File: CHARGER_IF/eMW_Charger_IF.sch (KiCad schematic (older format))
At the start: 9 parts

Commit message: Charger IF WIP
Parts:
- removed U?: SN74ACT08N, symbol SN74LS08N
- added C?: 10 uF / 25V / TH, symbol C
- added C?: 22 uF / 16V / TH, symbol C
- added J?: Booster_J1_J3, symbol Booster_J1_J3
- added J?: Booster_J4_J2, symbol Booster_J4_J2
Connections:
- net +5V: now also U?.12 (4A), U?.9 (3A), C?.1, J?.21 (P21)
- net 12V: now also C?.1
- net GND: now also U?.7 (GND), C?.2, C?.2, J?.22 (P22)
- net at U?.23 (RXI): now also J?.3 (P3)
- net at U?.24 (TXO): now also J?.4 (P4)
- net at U?.31 (A4-T2): now also J?.25 (P25)
- net at U?.32 (A5-MainsV): now also J?.26 (P26)
- net at U?.33 (A6-Analog-Spare-1): now also J?.27 (P27)
- net at U?.34 (A7-Analog-Spare-2): now also J?.28 (P28)
- net at U?.5 (A3-Uvio): now also J?.24 (P24)
- net at U?.7 (A1-V-Sense): now also J?.2 (P2)
- net at U?.8 (A0-C-Sense): now also J?.6 (P6)
- net at U?.~ (A2-Heat-Sink-Temp): now also J?.23 (P23)
- net at U?.12 (4A): now also J?.36 (P36)
- net at U?.2 (1B): now also J?.38 (P38)
- net at U?.5 (2B): now also J?.37 (P37)
- net at U?.9 (3A): now also J?.35 (P35)
- net at U?.2 (1B): now also J?.34 (P34)
- net at U?.5 (2B): now also J?.33 (P33)
- net at R?.1, R?.2: now also J?.39 (P39)
- net at R?.1, R?.2: now also J?.40 (P40)
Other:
- moved on the sheet: R?, U?

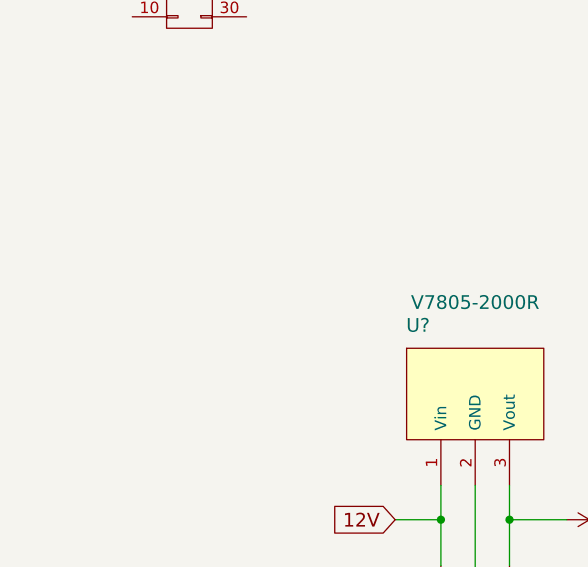
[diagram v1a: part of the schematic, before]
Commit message: Added URLS WIP
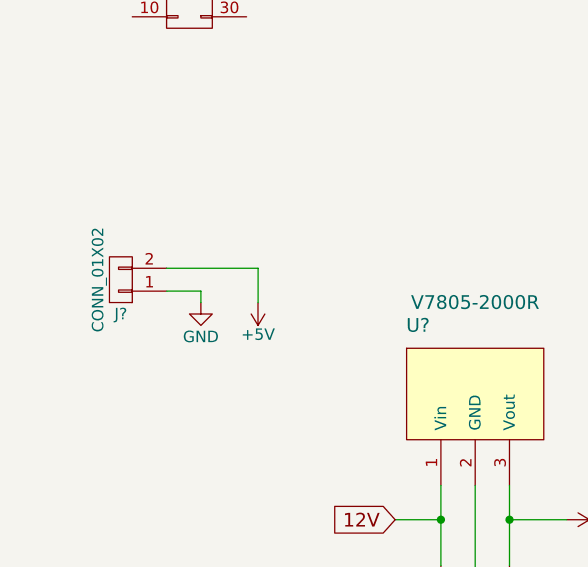
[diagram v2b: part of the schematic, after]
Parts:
- added J?: CONN_01X02, symbol CONN_01X02
- C?: Mouser PN (none) -> 810-FG26X7R1E106KRT6; Mouser URL (none) -> http://www.mouser.com/search/ProductDetail.aspx?R=0virtualk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
- C?: Mouser PN (none) -> 810-FG22X7R1E226MRT6; Mouser URL (none) -> http://www.mouser.com/search/ProductDetail.aspx?R=0virtualk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
- U? (x2): Mouser PN (none) -> 595-SN74ACT08N; Mouser URL (none) -> http://www.mouser.com/search/ProductDetail.aspx?R=0virtualk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
- U?: Mouser PN (none) -> 490-V7805-2000R; Mouser URL (none) -> http://www.mouser.com/search/ProductDetail.aspx?R=0virtualk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
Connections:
- net +5V: now also J?.2 (P2)
- net GND: now also J?.1 (P1)
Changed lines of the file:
@@
 F 2 "" H 7000 2700 60  0000 C CNN
 F 3 "" H 7000 2700 60  0000 C CNN
+F 4 "595-SN74ACT08N" H 7000 2700 60  0001 C CNN "Mouser PN"
+F 5 "http://www.mouser.com/search/ProductDetail.aspx?R=0virtualkey0virtualkeySN74ACT08N" H 7000 2700 60  0001 C CNN "Mouser URL"
 	1    7000 2700
 	-1   0    0    -1
@@
 F 2 "" H 7000 4850 60  0000 C CNN
 F 3 "" H 7000 4850 60  0000 C CNN
+F 4 "595-SN74ACT08N" H 7000 4850 60  0001 C CNN "Mouser PN"
+F 5 "http://www.mouser.com/search/ProductDetail.aspx?R=0virtualkey0virtualkeySN74ACT08N" H 7000 4850 60  0001 C CNN "Mouser URL"
 	1    7000 4850
 	-1   0    0    -1
@@
 F 2 "" H 2950 4450 60  0000 C CNN
 F 3 "" H 2950 4450 60  0000 C CNN
+F 4 "490-V7805-2000R" H 2950 4450 60  0001 C CNN "Mouser PN"
+F 5 "http://www.mouser.com/search/ProductDetail.aspx?R=0virtualkey0virtualkeyV7805-2000R" H 2950 4450 60  0001 C CNN "Mouser URL"
 	1    2950 4450
 	1    0    0    -1
@@
 F 2 "" H 2838 5200 50  0000 C CNN
 F 3 "" H 2800 5350 50  0000 C CNN
+F 4 "810-FG26X7R1E106KRT6" H 2800 5350 60  0001 C CNN "Mouser PN"
+F 5 "http://www.mouser.com/search/ProductDetail.aspx?R=0virtualkey0virtualkeyFG26X7R1E106KRT06" H 2800 5350 60  0001 C CNN "Mouser URL"
 	1    2800 5350
 	1    0    0    -1
@@
 F 2 "" H 3138 5200 50  0000 C CNN
 F 3 "" H 3100 5350 50  0000 C CNN
+F 4 "810-FG22X7R1E226MRT6" H 3100 5350 60  0001 C CNN "Mouser PN"
+F 5 "http://www.mouser.com/search/ProductDetail.aspx?R=0virtualkey0virtualkeyFG22X7R1E226MRT06" H 3100 5350 60  0001 C CNN "Mouser URL"
 	1    3100 5350
 	1    0    0    -1
@@
 	7600 5050 7950 5050
 Connection ~ 7950 5050
+$Comp
+L CONN_01X02 J?
+U 1 1 59765191
+P 1400 3950
+F 0 "J?" H 1400 4100 50  0000 C CNN
+F 1 "CONN_01X02" V 1500 3950 50  0000 C CNN
+F 2 "" H 1400 3950 50  0001 C CNN
+F 3 "" H 1400 3950 50  0001 C CNN
+	1    1400 3950
+	-1   0    0    1
+$EndComp
+$Comp
+L GND #PWR?
+U 1 1 597651CE
+P 1750 4050
+F 0 "#PWR?" H 1750 3800 50  0001 C CNN
+F 1 "GND" H 1750 3900 50  0000 C CNN
+F 2 "" H 1750 4050 50  0001 C CNN
+F 3 "" H 1750 4050 50  0001 C CNN
+	1    1750 4050
+	1    0    0    -1
+$EndComp
+$Comp
+L +5V #PWR?
+U 1 1 597651FC
+P 2000 4050
+F 0 "#PWR?" H 2000 3900 50  0001 C CNN
+F 1 "+5V" H 2000 4190 50  0000 C CNN
+F 2 "" H 2000 4050 50  0001 C CNN
+F 3 "" H 2000 4050 50  0001 C CNN
+	1    2000 4050
+	-1   0    0    1
+$EndComp
+Wire Wire Line
+	1750 4050 1750 4000
+Wire Wire Line
+	1750 4000 1600 4000
+Wire Wire Line
+	1600 3900 2000 3900
+Wire Wire Line
+	2000 3900 2000 4050
 $EndSCHEMATC

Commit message: Rough start on charger IF PCB
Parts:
- C1, C2: renamed from C?; footprint (none) -> Capacitors_THT:CP_Radial_D6.3mm_P2.50mm
- J1: renamed from J?; footprint (none) -> Pin_Headers:Pin_Header_Straight_1x02_Pitch2.54mm
- J2: renamed from J?; footprint (none) -> eMW_Charger:6-146256-0
- J3: renamed from J?; footprint (none) -> eMW_Charger:6-146256-0_40-31_20_11
- R1, R2, R3, R4: renamed from R?; footprint (none) -> Resistors_THT:R_Axial_DIN0204_L3.6mm_D1.6mm_P5.08mm_Horizontal
- U1: renamed from U?; footprint (none) -> eMW_Charger:V7805-2000R
- U2: renamed from U?; footprint (none) -> Pin_Headers:Pin_Header_Straight_2x10_Pitch2.54mm
- U3, U4: renamed from U?; footprint (none) -> Housings_DIP:DIP-14_W7.62mm
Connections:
- net +5V: no longer J1.2 (P2)
- net 12V renamed +12V
- net +12V: now also J1.2 (P2)
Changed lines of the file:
@@
 $EndDescr
 $Comp
-L ArduinoSocket U?
+L ArduinoSocket U2
 U 1 1 59742778
 P 4500 1850
-F 0 "U?" H 5250 2800 60  0000 C CNN
+F 0 "U2" H 5250 2800 60  0000 C CNN
 F 1 "ArduinoSocket" H 3900 2800 60  0000 C CNN
-F 2 "" H 4500 1500 60  0000 C CNN
+F 2 "Pin_Headers:Pin_Header_Straight_2x10_Pitch2.54mm" H 4500 1500 60  0001 C CNN
 F 3 "" H 4500 1500 60  0000 C CNN
 	1    4500 1850
@@
 $EndComp
 $Comp
-L SN74LS08N U?
+L SN74LS08N U3
 U 1 1 59742C3C
 P 7000 2700
-F 0 "U?" H 7200 3400 60  0000 C CNN
+F 0 "U3" H 7200 3400 60  0000 C CNN
 F 1 "SN74ACT08N" H 6600 3400 60  0000 C CNN
-F 2 "" H 7000 2700 60  0000 C CNN
+F 2 "Housings_DIP:DIP-14_W7.62mm" H 7000 2700 60  0001 C CNN
 F 3 "" H 7000 2700 60  0000 C CNN
 F 4 "595-SN74ACT08N" H 7000 2700 60  0001 C CNN "Mouser PN"
@@
 $EndComp
 $Comp
-L SN74LS08N U?
+L SN74LS08N U4
 U 1 1 59742C8F
 P 7000 4850
-F 0 "U?" H 7200 5550 60  0000 C CNN
+F 0 "U4" H 7200 5550 60  0000 C CNN
 F 1 "SN74ACT08N" H 6600 5550 60  0000 C CNN
-F 2 "" H 7000 4850 60  0000 C CNN
+F 2 "Housings_DIP:DIP-14_W7.62mm" H 7000 4850 60  0001 C CNN
 F 3 "" H 7000 4850 60  0000 C CNN
 F 4 "595-SN74ACT08N" H 7000 4850 60  0001 C CNN "Mouser PN"
@@
 $EndComp
 $Comp
-L R R?
+L R R4
 U 1 1 59742F49
 P 9500 2300
-F 0 "R?" H 9600 2250 50  0000 C CNN
+F 0 "R4" H 9600 2250 50  0000 C CNN
 F 1 "20k / 10% / TH" H 9900 2350 50  0000 C CNN
-F 2 "" V 9430 2300 50  0000 C CNN
+F 2 "Resistors_THT:R_Axial_DIN0204_L3.6mm_D1.6mm_P5.08mm_Horizontal" V 9430 2300 50  0001 C CNN
 F 3 "" H 9500 2300 50  0000 C CNN
 	1    9500 2300
@@
 $EndComp
 $Comp
-L R R?
+L R R3
 U 1 1 59742FA5
 P 9500 1700
-F 0 "R?" H 9600 1650 50  0000 C CNN
+F 0 "R3" H 9600 1650 50  0000 C CNN
 F 1 "10k / 10% / TH" H 9900 1750 50  0000 C CNN
-F 2 "" V 9430 1700 50  0000 C CNN
+F 2 "Resistors_THT:R_Axial_DIN0204_L3.6mm_D1.6mm_P5.08mm_Horizontal" V 9430 1700 50  0001 C CNN
 F 3 "" H 9500 1700 50  0000 C CNN
 	1    9500 1700
@@
 $EndComp
 $Comp
-L R R?
+L R R1
 U 1 1 59743279
 P 8600 1800
-F 0 "R?" H 8700 1750 50  0000 C CNN
+F 0 "R1" H 8700 1750 50  0000 C CNN
 F 1 "10k / 10% / TH" H 9000 1850 50  0000 C CNN
-F 2 "" V 8530 1800 50  0000 C CNN
+F 2 "Resistors_THT:R_Axial_DIN0204_L3.6mm_D1.6mm_P5.08mm_Horizontal" V 8530 1800 50  0001 C CNN
 F 3 "" H 8600 1800 50  0000 C CNN
 	1    8600 1800
@@
 $EndComp
 $Comp
-L R R?
+L R R2
 U 1 1 597432A0
 P 8600 2300
-F 0 "R?" H 8700 2250 50  0000 C CNN
+F 0 "R2" H 8700 2250 50  0000 C CNN
 F 1 "20k / 10% / TH" H 9000 2350 50  0000 C CNN
-F 2 "" V 8530 2300 50  0000 C CNN
+F 2 "Resistors_THT:R_Axial_DIN0204_L3.6mm_D1.6mm_P5.08mm_Horizontal" V 8530 2300 50  0001 C CNN
 F 3 "" H 8600 2300 50  0000 C CNN
 	1    8600 2300
@@
 $EndComp
 $Comp
-L V7805-2000R U?
+L V7805-2000R U1
 U 1 1 5974381A
 P 2950 4450
-F 0 "U?" H 2700 4750 60  0000 C CNN
+F 0 "U1" H 2700 4750 60  0000 C CNN
 F 1 "V7805-2000R" H 2950 4850 60  0000 C CNN
-F 2 "" H 2950 4450 60  0000 C CNN
+F 2 "eMW_Charger:V7805-2000R" H 2950 4450 60  0001 C CNN
 F 3 "" H 2950 4450 60  0000 C CNN
 F 4 "490-V7805-2000R" H 2950 4450 60  0001 C CNN "Mouser PN"
@@
 	1    0    0    -1
 $EndComp
-Text GLabel 2600 5000 0    60   Input ~ 0
-12V
-$Comp
-L GND #PWR?
+$Comp
+L GND #PWR01
 U 1 1 5974397D
 P 2950 5750
-F 0 "#PWR?" H 2950 5500 50  0001 C CNN
+F 0 "#PWR01" H 2950 5500 50  0001 C CNN
 F 1 "GND" H 2950 5600 50  0000 C CNN
 F 2 "" H 2950 5750 50  0000 C CNN
@@
 $EndComp
 $Comp
-L +5V #PWR?
+L +5V #PWR02
 U 1 1 59743A17
 P 3350 5000
-F 0 "#PWR?" H 3350 4850 50  0001 C CNN
+F 0 "#PWR02" H 3350 4850 50  0001 C CNN
 F 1 "+5V" H 3350 5140 50  0000 C CNN
 F 2 "" H 3350 5000 50  0000 C CNN
@@
 $EndComp
 $Comp
-L +5V #PWR?
+L +5V #PWR03
 U 1 1 59743C47
 P 6750 1850
-F 0 "#PWR?" H 6750 1700 50  0001 C CNN
+F 0 "#PWR03" H 6750 1700 50  0001 C CNN
 F 1 "+5V" H 6750 1990 50  0000 C CNN
 F 2 "" H 6750 1850 50  0000 C CNN
@@
 $EndComp
 $Comp
-L +5V #PWR?
+L +5V #PWR04
 U 1 1 59743C6D
 P 6750 4000
-F 0 "#PWR?" H 6750 3850 50  0001 C CNN
+F 0 "#PWR04" H 6750 3850 50  0001 C CNN
 F 1 "+5V" H 6750 4140 50  0000 C CNN
 F 2 "" H 6750 4000 50  0000 C CNN
@@
 $EndComp
 $Comp
-L GND #PWR?
+L GND #PWR05
 U 1 1 59743F57
 P 6750 3600
-F 0 "#PWR?" H 6750 3350 50  0001 C CNN
+F 0 "#PWR05" H 6750 3350 50  0001 C CNN
 F 1 "GND" H 6750 3450 50  0000 C CNN
 F 2 "" H 6750 3600 50  0000 C CNN
@@
 $EndComp
 $Comp
-L +5V #PWR?
+L +5V #PWR06
 U 1 1 597440FC
 P 7950 4350
-F 0 "#PWR?" H 7950 4200 50  0001 C CNN
+F 0 "#PWR06" H 7950 4200 50  0001 C CNN
 F 1 "+5V" H 7950 4490 50  0000 C CNN
 F 2 "" H 7950 4350 50  0000 C CNN
@@
 $EndComp
 $Comp
-L GND #PWR?
+L GND #PWR07
 U 1 1 59744821
 P 9500 2550
-F 0 "#PWR?" H 9500 2300 50  0001 C CNN
+F 0 "#PWR07" H 9500 2300 50  0001 C CNN
 F 1 "GND" H 9500 2400 50  0000 C CNN
 F 2 "" H 9500 2550 50  0000 C CNN
@@
 $EndComp
 $Comp
-L GND #PWR?
+L GND #PWR08
 U 1 1 59744980
 P 3200 2550
-F 0 "#PWR?" H 3200 2300 50  0001 C CNN
+F 0 "#PWR08" H 3200 2300 50  0001 C CNN
 F 1 "GND" H 3200 2400 50  0000 C CNN
 F 2 "" H 3200 2550 50  0000 C CNN
@@
 $EndComp
 $Comp
-L GND #PWR?
+L GND #PWR09
 U 1 1 59744C12
 P 6750 5750
-F 0 "#PWR?" H 6750 5500 50  0001 C CNN
+F 0 "#PWR09" H 6750 5500 50  0001 C CNN
 F 1 "GND" H 6750 5600 50  0000 C CNN
 F 2 "" H 6750 5750 50  0000 C CNN
@@
 $EndComp
 $Comp
-L +5V #PWR?
+L +5V #PWR010
 U 1 1 59744F3B
 P 8000 2100
-F 0 "#PWR?" H 8000 1950 50  0001 C CNN
+F 0 "#PWR010" H 8000 1950 50  0001 C CNN
 F 1 "+5V" H 8000 2240 50  0000 C CNN
 F 2 "" H 8000 2100 50  0000 C CNN
@@
 $EndComp
 $Comp
-L Booster_J1_J3 J?
+L Booster_J1_J3 J2
 U 1 1 59753F21
 P 1700 2350
-F 0 "J?" H 1700 2900 50  0000 C CNN
+F 0 "J2" H 1700 2900 50  0000 C CNN
 F 1 "Booster_J1_J3" V 1700 2350 50  0000 C CNN
-F 2 "" H 1700 1150 50  0001 C CNN
+F 2 "eMW_Charger:6-146256-0" H 1700 1150 50  0001 C CNN
 F 3 "" H 1700 1150 50  0001 C CNN
 	1    1700 2350
@@
 $EndComp
 $Comp
-L Booster_J4_J2 J?
+L Booster_J4_J2 J3
 U 1 1 59753F62
 P 10450 3100
-F 0 "J?" H 10450 3650 50  0000 C CNN
+F 0 "J3" H 10450 3650 50  0000 C CNN
 F 1 "Booster_J4_J2" V 10450 3100 50  0000 C CNN
-F 2 "" H 10450 1900 50  0001 C CNN
+F 2 "eMW_Charger:6-146256-0_40-31_20_11" H 10450 1900 50  0001 C CNN
 F 3 "" H 10450 1900 50  0001 C CNN
 	1    10450 3100
@@
 Connection ~ 9500 2050
 $Comp
-L GND #PWR?
+L GND #PWR011
 U 1 1 59757692
 P 8600 2500
-F 0 "#PWR?" H 8600 2250 50  0001 C CNN
+F 0 "#PWR011" H 8600 2250 50  0001 C CNN
 F 1 "GND" H 8600 2350 50  0000 C CNN
 F 2 "" H 8600 2500 50  0000 C CNN
@@
 	1350 1550 1350 2000
 $Comp
-L +5V #PWR?
+L +5V #PWR012
 U 1 1 597590C9
 P 2100 1750
-F 0 "#PWR?" H 2100 1600 50  0001 C CNN
+F 0 "#PWR012" H 2100 1600 50  0001 C CNN
 F 1 "+5V" H 2100 1890 50  0000 C CNN
 F 2 "" H 2100 1750 50  0000 C CNN
@@
 	2100 1900 2100 1750
 $Comp
-L GND #PWR?
+L GND #PWR013
 U 1 1 597592AC
 P 2300 1750
-F 0 "#PWR?" H 2300 1500 50  0001 C CNN
+F 0 "#PWR013" H 2300 1500 50  0001 C CNN
 F 1 "GND" H 2300 1600 50  0000 C CNN
 F 2 "" H 2300 1750 50  0000 C CNN
@@
 	6000 1350 5650 1350
 $Comp
-L C C?
+L C C1
 U 1 1 59759984
 P 2800 5350
-F 0 "C?" H 2550 5450 50  0000 L CNN
+F 0 "C1" H 2550 5450 50  0000 L CNN
 F 1 "10 uF / 25V / TH" H 2000 5250 50  0000 L CNN
-F 2 "" H 2838 5200 50  0000 C CNN
+F 2 "Capacitors_THT:CP_Radial_D6.3mm_P2.50mm" H 2838 5200 50  0001 C CNN
 F 3 "" H 2800 5350 50  0000 C CNN
 F 4 "810-FG26X7R1E106KRT6" H 2800 5350 60  0001 C CNN "Mouser PN"
@@
 $EndComp
 $Comp
-L C C?
+L C C2
 U 1 1 597599F0
 P 3100 5350
-F 0 "C?" H 3125 5450 50  0000 L CNN
+F 0 "C2" H 3125 5450 50  0000 L CNN
 F 1 "22 uF / 16V / TH" H 3125 5250 50  0000 L CNN
-F 2 "" H 3138 5200 50  0000 C CNN
+F 2 "Capacitors_THT:CP_Radial_D6.3mm_P2.50mm" H 3138 5200 50  0001 C CNN
 F 3 "" H 3100 5350 50  0000 C CNN
 F 4 "810-FG22X7R1E226MRT6" H 3100 5350 60  0001 C CNN "Mouser PN"
@@
 Connection ~ 7950 5050
 $Comp
-L CONN_01X02 J?
+L CONN_01X02 J1
 U 1 1 59765191
 P 1400 3950
-F 0 "J?" H 1400 4100 50  0000 C CNN
+F 0 "J1" H 1400 4100 50  0000 C CNN
 F 1 "CONN_01X02" V 1500 3950 50  0000 C CNN
-F 2 "" H 1400 3950 50  0001 C CNN
+F 2 "Pin_Headers:Pin_Header_Straight_1x02_Pitch2.54mm" H 1400 3950 50  0001 C CNN
 F 3 "" H 1400 3950 50  0001 C CNN
 	1    1400 3950
@@
 $EndComp
 $Comp
-L GND #PWR?
+L GND #PWR014
 U 1 1 597651CE
 P 1750 4050
-F 0 "#PWR?" H 1750 3800 50  0001 C CNN
+F 0 "#PWR014" H 1750 3800 50  0001 C CNN
 F 1 "GND" H 1750 3900 50  0000 C CNN
 F 2 "" H 1750 4050 50  0001 C CNN
@@
 	1    0    0    -1
 $EndComp
-$Comp
-L +5V #PWR?
-U 1 1 597651FC
+Wire Wire Line
+	1750 4050 1750 4000
+Wire Wire Line
+	1750 4000 1600 4000
+Wire Wire Line
+	1600 3900 2000 3900
+Wire Wire Line
+	2000 3900 2000 4050
+$Comp
+L +12V #PWR?
+U 1 1 5976DD79
+P 2600 5000
+F 0 "#PWR?" H 2600 4850 50  0001 C CNN
+F 1 "+12V" H 2600 5140 50  0000 C CNN
+F 2 "" H 2600 5000 50  0000 C CNN
+F 3 "" H 2600 5000 50  0000 C CNN
+	1    2600 5000
+	0    -1   -1   0
+$EndComp
+$Comp
+L +12V #PWR?
+U 1 1 5976DDB2
 P 2000 4050
 F 0 "#PWR?" H 2000 3900 50  0001 C CNN
-F 1 "+5V" H 2000 4190 50  0000 C CNN
-F 2 "" H 2000 4050 50  0001 C CNN
-F 3 "" H 2000 4050 50  0001 C CNN
+F 1 "+12V" H 2000 4190 50  0000 C CNN
+F 2 "" H 2000 4050 50  0000 C CNN
+F 3 "" H 2000 4050 50  0000 C CNN
 	1    2000 4050
 	-1   0    0    1
 $EndComp
-Wire Wire Line
-	1750 4050 1750 4000
-Wire Wire Line
-	1750 4000 1600 4000
-Wire Wire Line
-	1600 3900 2000 3900
-Wire Wire Line
-	2000 3900 2000 4050
 $EndSCHEMATC

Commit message: Charger IF WIP
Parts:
- removed U2: ArduinoSocket, Pin_Headers:Pin_Header_Straight_2x10_Pitch2.54mm, symbol ArduinoSocket
- added J? (x2): CONN_02X10, symbol CONN_02X10
- added U?: Arduino-Socket, symbol Arduino-Socket
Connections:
- net GND: now also J?.11 (P11)
- net at U4.6 (2Y): now also J?.9 (P9)
- net at U4.3 (1Y): now also J?.10 (P10)
- net at U3.8 (3Y): now also J?.7 (P7)
- net at U3.11 (4Y): now also J?.8 (P8)
- net at U3.6 (2Y): now also J?.5 (P5)
- net at U3.3 (1Y): now also J?.4 (P4)
- net at R1.1: now also J?.6 (P6)
- net at R3.1: now also J?.3 (P3)
- net at J2.3 (P3): now also J?.1 (P1)
- net at J2.4 (P4): now also J?.2 (P2)
- net at J2.25 (P25): now also J?.16 (P16)
- net at J2.26 (P26): now also J?.18 (P18)
- net at J2.27 (P27): now also J?.19 (P19)
- net at J2.28 (P28): now also J?.20 (P20)
- net at J2.24 (P24): now also J?.14 (P14)
- net at J2.2 (P2): now also J?.12 (P12)
- net at J2.6 (P6): now also J?.17 (P17)
- net at J2.23 (P23): now also J?.13 (P13)
- net at J2.5 (P5): now also J?.15 (P15)
- new net: J?.12 (P12), U?.12 (D10)
- new net: J?.9 (P9), U?.13 (D9)
- new net: J?.10 (P10), U?.14 (D8)
- new net: J?.7 (P7), U?.16 (D6)
- new net: J?.8 (P8), U?.17 (D5)
- new net: J?.5 (P5), U?.18 (D4)
- new net: J?.6 (P6), U?.19 (D3)
- new net: J?.3 (P3), U?.20 (D2)
- new net: J?.11 (P11), U?.21 (GND)
- new net: J?.4 (P4), U?.22 (RST)
- new net: J?.1 (P1), U?.23 (RXI)
- new net: J?.2 (P2), U?.24 (TXD)
- new net: J?.15 (P15), U?.31 (A4)
- new net: J?.13 (P13), U?.32 (A5)
- new net: J?.20 (P20), U?.33 (A6)
- new net: J?.19 (P19), U?.34 (A7)
- new net: J?.14 (P14), U?.5 (A3)
- new net: J?.16 (P16), U?.6 (A2)
- new net: J?.17 (P17), U?.7 (A1)
- new net: J?.18 (P18), U?.8 (A0)
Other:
- note added: "A5: Mains V\nA4: Ts\nA6: Th\nA7: bC"
- note added: "C-Sense"
- note added: "Charge Current PWM"
- note added: "Fan Relay"
- note added: "Green Btn"
- note added: "Heat-Sink Temp"
- note added: "Jin"
- note added: "Max Current PWM"
- note added: "Red Btn"
- note added: "Shutdown"
- note added: "Uvio"
- note added: "V-Sense"
- moved on the sheet: C1, C2, J1, J2, J3, R1, R2, R3, R4, U1, U3, U4

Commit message: Charger IF WIP
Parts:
- J4, J5: renamed from J?; footprint (none) -> Pin_Headers:Pin_Header_Straight_2x10_Pitch2.54mm
- U2: renamed from U?; footprint (none) -> eMW_Charger:eMW-Control-Board-Arduino-Header
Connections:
- net GND: now also J4.11 (P11), U2.21 (GND)
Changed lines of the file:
@@
 $EndComp
 $Comp
-L +12V #PWR?
+L +12V #PWR015
 U 1 1 5976DD79
 P 3625 6275
-F 0 "#PWR?" H 3625 6125 50  0001 C CNN
+F 0 "#PWR015" H 3625 6125 50  0001 C CNN
 F 1 "+12V" H 3625 6415 50  0000 C CNN
 F 2 "" H 3625 6275 50  0000 C CNN
@@
 $EndComp
 $Comp
-L +12V #PWR?
+L +12V #PWR016
 U 1 1 5976DDB2
 P 2675 6325
-F 0 "#PWR?" H 2675 6175 50  0001 C CNN
+F 0 "#PWR016" H 2675 6175 50  0001 C CNN
 F 1 "+12V" H 2675 6465 50  0000 C CNN
 F 2 "" H 2675 6325 50  0000 C CNN
@@
 $EndComp
 $Comp
-L Arduino-Socket U?
+L Arduino-Socket U2
 U 1 1 59792C6A
 P 2850 4225
-F 0 "U?" H 1650 5125 60  0000 C CNN
+F 0 "U2" H 1650 5125 60  0000 C CNN
 F 1 "Arduino-Socket" H 1950 5275 60  0000 C CNN
-F 2 "" H 2750 4575 60  0001 C CNN
+F 2 "eMW_Charger:eMW-Control-Board-Arduino-Header" H 2750 4575 60  0001 C CNN
 F 3 "" H 2750 4575 60  0001 C CNN
 	1    2850 4225
@@
 A5: Mains V\nA4: Ts\nA6: Th\nA7: bC
 $Comp
-L CONN_02X10 J?
+L CONN_02X10 J4
 U 1 1 59793B0C
 P 2700 4275
-F 0 "J?" H 2700 4825 50  0000 C CNN
+F 0 "J4" H 2700 4825 50  0000 C CNN
 F 1 "CONN_02X10" V 2700 4275 50  0000 C CNN
-F 2 "" H 2700 3075 50  0001 C CNN
+F 2 "Pin_Headers:Pin_Header_Straight_2x10_Pitch2.54mm" H 2700 3075 50  0001 C CNN
 F 3 "" H 2700 3075 50  0001 C CNN
 	1    2700 4275
@@
 $EndComp
 $Comp
-L CONN_02X10 J?
+L CONN_02X10 J5
 U 1 1 59796F8F
 P 4400 1800
-F 0 "J?" H 4400 2350 50  0000 C CNN
+F 0 "J5" H 4400 2350 50  0000 C CNN
 F 1 "CONN_02X10" V 4400 1800 50  0000 C CNN
-F 2 "" H 4400 600 50  0001 C CNN
+F 2 "Pin_Headers:Pin_Header_Straight_2x10_Pitch2.54mm" H 4400 600 50  0001 C CNN
 F 3 "" H 4400 600 50  0001 C CNN
 	1    4400 1800
@@
 	6150 1700 6150 1700
 Wire Wire Line
-	6150 1700 6150 2350
+	6150 1600 6150 2350
 Wire Wire Line
 	6150 2350 6300 2350
 Wire Wire Line
-	6300 2600 6050 2600
-Wire Wire Line
-	6050 2600 6050 1800
-Wire Wire Line
-	6050 1800 6050 1800
-Wire Wire Line
-	6300 2850 5950 2850
-Wire Wire Line
-	5950 2850 5950 1900
-Wire Wire Line
-	5950 1900 5950 1900
-Wire Wire Line
-	5850 2000 5850 4250
+	6050 2600 6300 2600
+Wire Wire Line
+	6050 1650 6050 2600
+Wire Wire Line
+	5950 2850 6300 2850
+Wire Wire Line
+	5950 1700 5950 2850
+Wire Wire Line
+	5850 1750 5850 4250
 Wire Wire Line
 	5850 4250 6300 4250
 Wire Wire Line
-	6300 4500 5750 4500
-Wire Wire Line
-	5750 4500 5750 2100
+	5750 4500 6300 4500
+Wire Wire Line
+	5750 1800 5750 4500
 Wire Wire Line
 	3625 6275 3825 6275
 Wire Wire Line
-	3825 6125 3825 6275
-Wire Wire Line
-	3825 6275 3825 6475
-Wire Wire Line
-	3975 6125 3975 6875
-Wire Wire Line
-	3975 6875 3975 7025
+	3825 6125 3825 6475
+Wire Wire Line
+	3975 6125 3975 7025
 Wire Wire Line
 	6500 1600 6850 1600
@@
 	6850 5500 6350 5500
 Wire Wire Line
-	7750 4100 7750 4200
-Wire Wire Line
-	7750 4200 7750 4450
-Wire Wire Line
-	7750 4450 7750 4700
-Wire Wire Line
-	7750 4700 7750 4800
-Wire Wire Line
-	7750 4800 7750 4950
-Wire Wire Line
-	7750 4950 7750 5050
+	7750 4100 7750 5050
 Wire Wire Line
 	7750 4200 7450 4200
@@
 	7450 2050 7750 2050
 Wire Wire Line
-	7750 1850 7750 2050
-Wire Wire Line
-	7750 2050 7750 2300
-Wire Wire Line
-	7750 2300 7750 2550
-Wire Wire Line
-	7750 2550 7750 2800
+	7750 1850 7750 2800
 Wire Wire Line
 	7750 2300 7450 2300
@@
 Connection ~ 7750 2550
 Wire Wire Line
-	8150 1700 8150 1750
-Wire Wire Line
-	8150 1750 8150 1900
-Wire Wire Line
-	9100 1600 9100 1800
-Wire Wire Line
-	9100 1800 9100 1900
+	8150 1700 8150 1900
+Wire Wire Line
+	9100 1600 9100 1900
 Wire Wire Line
 	8150 2250 8150 2200
@@
 	2550 1950 2400 1950
 Wire Wire Line
-	4125 6125 4125 6275
-Wire Wire Line
-	4125 6275 4125 6475
+	4125 6125 4125 6475
 Wire Wire Line
 	4125 6275 4375 6275
@@
 	4125 6875 4125 6775
 Wire Wire Line
-	3825 6875 3975 6875
-Wire Wire Line
-	3975 6875 4125 6875
+	3825 6875 4125 6875
 Connection ~ 3975 6875
 Wire Wire Line
@@
 	4650 1550 4900 1550
 Wire Wire Line
-	5750 2100 5750 1800
-Wire Wire Line
 	5750 1800 4150 1800
 Wire Wire Line
 	4150 1800 4150 1750
 Wire Wire Line
-	5850 2000 5850 1750
-Wire Wire Line
 	5850 1750 4650 1750
 Wire Wire Line
-	5950 1900 5950 1700
-Wire Wire Line
 	5950 1700 4150 1700
 Wire Wire Line
 	4150 1700 4150 1650
 Wire Wire Line
-	6050 1800 6050 1650
-Wire Wire Line
 	6050 1650 4650 1650
 Wire Wire Line
-	6150 1700 6150 1600
-Wire Wire Line
 	6150 1600 4150 1600
 Wire Wire Line
@@
 Wire Wire Line
 	4850 1300 9100 1300
+$Comp
+L GND #PWR017
+U 1 1 5979CA5D
+P 1500 3850
+F 0 "#PWR017" H 1500 3600 50  0001 C CNN
+F 1 "GND" H 1500 3700 50  0000 C CNN
+F 2 "" H 1500 3850 50  0001 C CNN
+F 3 "" H 1500 3850 50  0001 C CNN
+	1    1500 3850
+	0    1    1    0
+$EndComp
+Wire Wire Line
+	1500 3850 2100 3850
+Wire Wire Line
+	2100 3850 2100 3900
+Connection ~ 2100 3900
 $EndSCHEMATC
